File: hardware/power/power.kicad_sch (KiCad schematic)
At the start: 30 parts, among them J1 SF6, J2 SF6, J3 PinHeader2x4, J4 PinHeader2x4, J5 PinHeader2x4, J6 SF6, J7 SF6, J8 SF6, Q1 ISC022N10NM6, Q2 ISC022N10NM6, Q3 ISC022N10NM6, Q4 ISC022N10NM6, Q5 ISC022N10NM6, Q6 ISC022N10NM6

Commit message: intermediate commit, some changes needed before first purchase
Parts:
- removed H2, H3, H4: HoleM3_ISO14580, MountingHole:MountingHole_3.2mm_M3_ISO14580, symbol Mechanical:MountingHole
- removed J3, J4, J5: PinHeader2x4, Connector_PinHeader_1.00mm:PinHeader_2x04_P1.00mm_Vertical_SMD, symbol Connector_Generic:Conn_02x04_Odd_Even
- removed Q1, Q2, Q3, Q4, Q5, Q6: ISC022N10NM6, Package_SO:PowerPAK_SO-8_Single, symbol Transistor_FET:Q_NMOS_SSSGD_AvalancheRated
- removed R2, R3, R4, R5, R6: 500u, Resistor_SMD:R_Shunt_Vishay_WSKW0612, symbol Device:R_Shunt
- removed TH2, TH3: NTC 10k, Resistor_SMD:R_0402_1005Metric, symbol Device:Thermistor_NTC
- added H102, H103, H104: HoleM2_ISO14580, MountingHole:MountingHole_2.2mm_M2_ISO14580, symbol Mechanical:MountingHole
- added J103, J104, J105, J111: PinHeader2x2, Connector_PinHeader_1.00mm:PinHeader_2x02_P1.00mm_Vertical_SMD, symbol Connector_Generic:Conn_02x02_Odd_Even
- added J109, J110: SF6, Connector_Wire:SolderWirePad_1x01_SMD_3x6mm, symbol Connector_Generic:Conn_01x01
- added R102, R103: 200u, mcrmv:WSK1216, symbol Device:R_Shunt
- H101: renamed from H1; value HoleM3_ISO14580 -> HoleM2_ISO14580; footprint MountingHole:MountingHole_3.2mm_M3_ISO14580 -> MountingHole:MountingHole_2.2mm_M2_ISO14580
- R101: renamed from R1; value 500u -> 200u; footprint Resistor_SMD:R_Shunt_Vishay_WSKW0612 -> mcrmv:WSK1216; MPN WSKW0612L5000FEA -> WSK1216L2000FEA
- renumbered FID1 to FID101, FID2 to FID102, FID3 to FID103, J1 to J101, J2 to J102, J6 to J106, J7 to J107, J8 to J108, TH1 to TH101
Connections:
- net NTC1- is gone; now on net GND: TH101.1
- net +80V: now also J109.1 (Pin_1)
- net GH1: now also J103.2 (Pin_2)
- net GH2: now also J104.2 (Pin_2)
- net GH3: now also J105.2 (Pin_2)
- net GL1: now also J103.4 (Pin_4)
- net GL2: now also J104.4 (Pin_4)
- net GL3: now also J105.4 (Pin_4)
- net GND: now also J110.1 (Pin_1), J111.1 (Pin_1), J111.2 (Pin_2), J111.4 (Pin_4)
- net NTC1+: now also J111.3 (Pin_3)
- net P1: now also R101.4; no longer R101.1
- net P1_TAB: now also R101.1; no longer R101.4
- net P2: now also R102.4
- net P2_TAB: now also R102.1
- net P3: now also R103.4
- net P3_TAB: now also R103.1
- net S1_N: now also R101.2, J103.3 (Pin_3); no longer R101.3
- net S1_P: now also R101.3, J103.1 (Pin_1); no longer R101.2
- net S2_N: now also J104.3 (Pin_3), R102.2
- net S2_P: now also J104.1 (Pin_1), R102.3
- net S3_N: now also J105.3 (Pin_3), R103.2
- net S3_P: now also J105.1 (Pin_1), R103.3
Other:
- added sheet fets0 (fets.kicad_sch)
- added sheet fets1 (fets.kicad_sch)
- moved on the sheet: J101, J102, R101

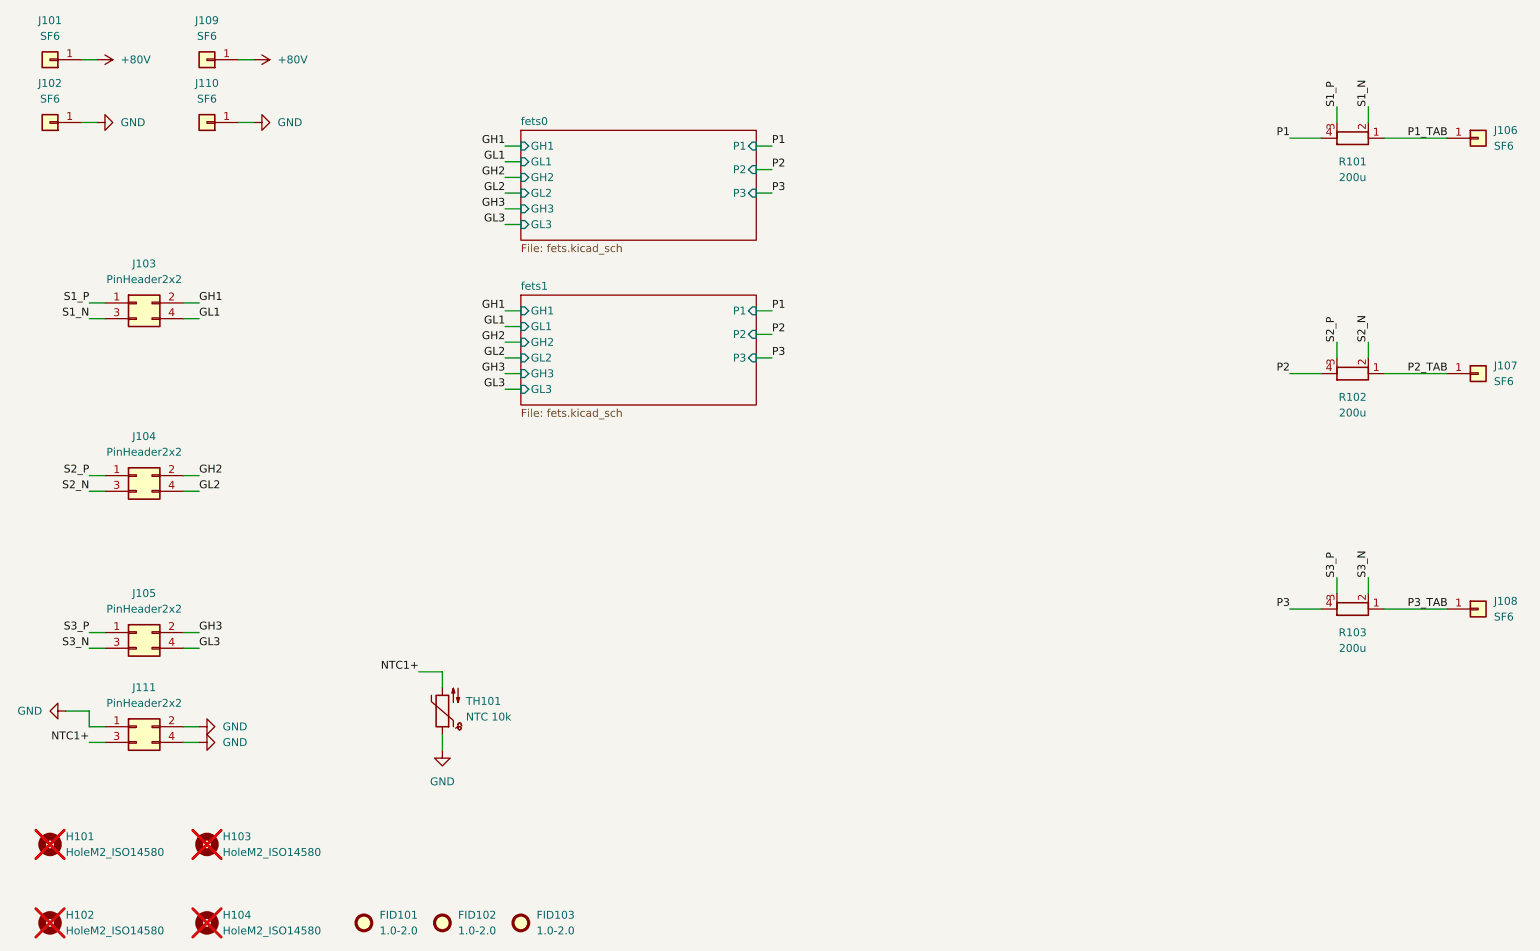
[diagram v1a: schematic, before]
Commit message: added connectors to add individual current paths, filled with ntcs, plotted pdf, updated screenshots
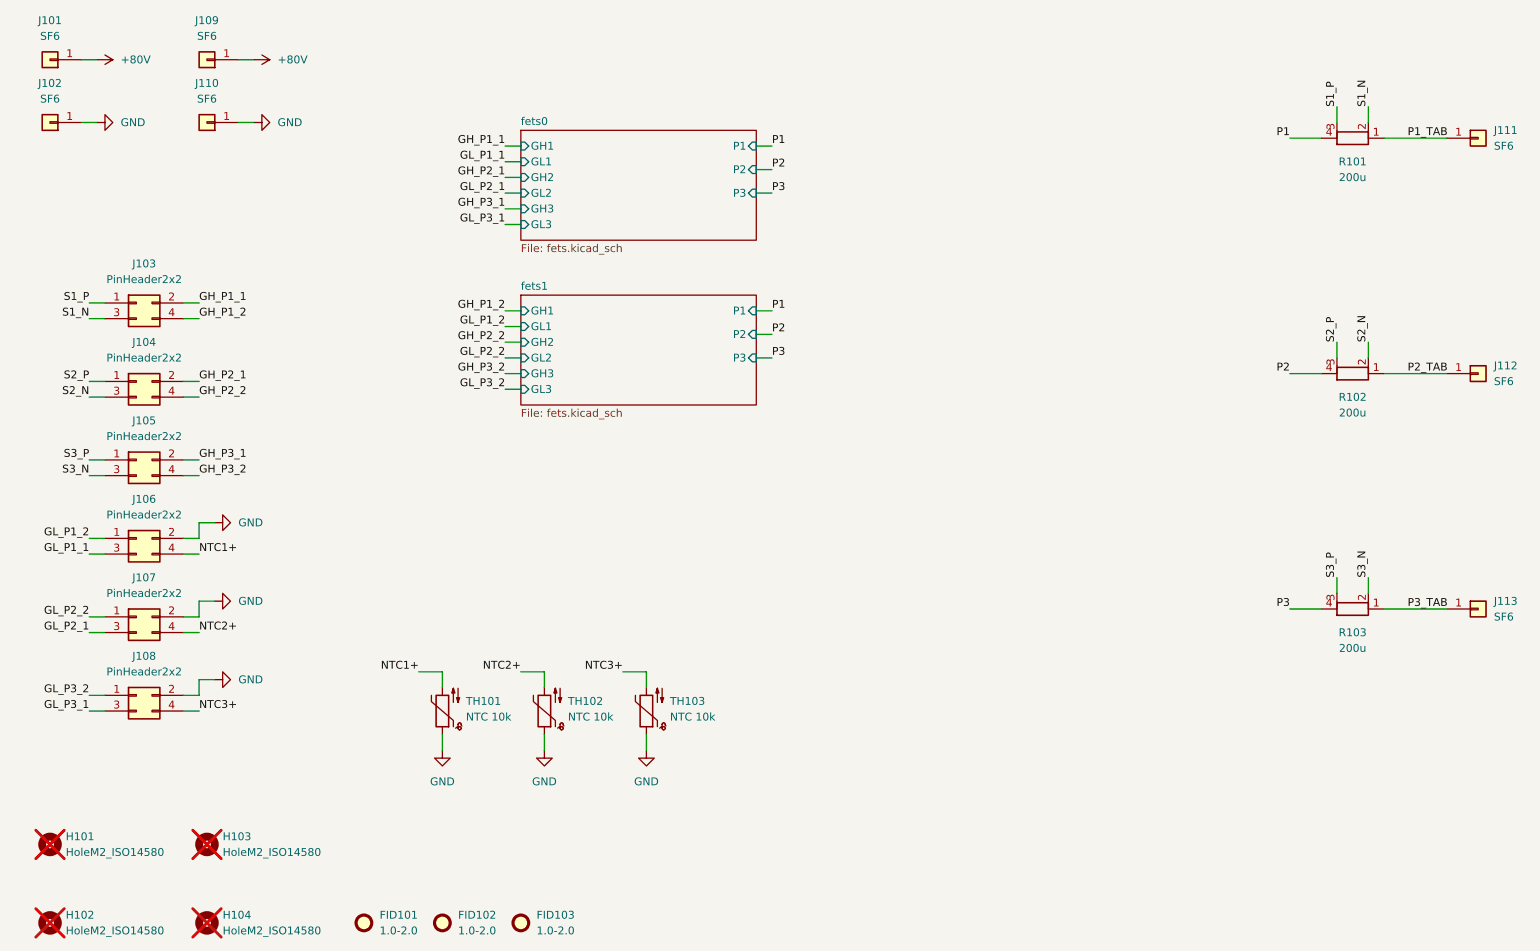
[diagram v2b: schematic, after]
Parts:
- added J106, J107: PinHeader2x2, Connector_PinHeader_1.00mm:PinHeader_2x02_P1.00mm_Vertical_SMD, symbol Connector_Generic:Conn_02x02_Odd_Even
- added TH102, TH103: NTC 10k, Resistor_SMD:R_0402_1005Metric, symbol Device:Thermistor_NTC
- renumbered J111 to J108, J106 to J111, J107 to J112, J108 to J113
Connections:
- net GND: now also J106.2 (Pin_2), J107.2 (Pin_2), TH102.1, TH103.1; no longer J108.1 (Pin_1), J108.4 (Pin_4)
- net NTC1+: now also J106.4 (Pin_4); no longer J108.3 (Pin_3)
- net GH1 renamed GH_P1_1
- net GH2 renamed GH_P2_1
- net GH3 renamed GH_P3_1
- net GL1 renamed GH_P1_2
- net GL2 renamed GH_P2_2
- net GL3 renamed GH_P3_2
- new net GL_P1_1: J106.3 (Pin_3)
- new net GL_P1_2: J106.1 (Pin_1)
- new net GL_P2_1: J107.3 (Pin_3)
- new net GL_P2_2: J107.1 (Pin_1)
- new net GL_P3_1: J108.3 (Pin_3)
- new net GL_P3_2: J108.1 (Pin_1)
- new net NTC2+: J107.4 (Pin_4), TH102.2
- new net NTC3+: J108.4 (Pin_4), TH103.2
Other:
- company: openmc -> github.com/arminstr
- moved on the sheet: J104, J105, J108
